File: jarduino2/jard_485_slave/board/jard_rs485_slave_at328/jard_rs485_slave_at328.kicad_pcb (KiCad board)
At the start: 2 copper layers, 80 x 30 mm, 72 parts, among them J1 BUS_IN, J2 BUS_OUT, J3 Débit, J4 Niveaux, J6 EV1, J7 ISCP, Q1 BPC_FMMT38C, Q2 BPC_FMMT38C, Q4 BPC_FMMT38C, Q6 BPC_IPP034N03L, U1 BPC_Alim5V, U2 MAX485E, U5 ATmega328P-A, U6 BPC_DHT22, Y1 Resonator

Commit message: Nouvel essai de routage avec en + LEDs
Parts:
- removed TP20, TP21: TestPoint, TestPoint:TestPoint_Pad_D1.5mm
- added D1: LED, LED_SMD:LED_0805_2012Metric_Pad1.15x1.40mm_HandSolder, B.Cu at (102.6, 44.6)
- added D3: LED, LED_THT:LED_D3.0mm_FlatTop, B.Cu at (103.8, 48.6)
- added R12: 220, Resistor_SMD:R_0805_2012Metric_Pad1.20x1.40mm_HandSolder, B.Cu at (87.8, 60.4)
- C13, C5, C8, C9, U5, Y1: moved to B.Cu
- R26: moved to F.Cu
- moved R17 40.5 mm to (125.2, 41.8), turned to 0 degrees
- moved TP11 38.2 mm to (80.4, 44.8), turned to 0 degrees
- moved Q6 38.0 mm to (126.3, 44.2), turned to 180 degrees
- moved D8 32.8 mm to (80.0, 48.9), turned to 90 degrees
- moved Y1 32.0 mm to (93.2, 67.2), turned to 0 degrees
- moved C8 31.2 mm to (93.6, 53.8), turned to 0 degrees
- moved Q4 29.4 mm to (116.1, 45.2), turned to 0 degrees
- moved R15 29.1 mm to (113.0, 45.2)
- moved D7 27.9 mm to (126.8, 67.5), turned to 180 degrees
- moved C9 26.5 mm to (95.9, 66.9)
- moved U5 25.7 mm to (96.3, 60.0)
- moved J6 25.6 mm to (121.2, 52.2), turned to 90 degrees
- moved C13 24.9 mm to (96.7, 53.9), turned to 180 degrees
- moved R7 24.8 mm to (84.4, 49.6), turned to 180 degrees
- moved R26 24.0 mm to (97.2, 60.4), turned to 180 degrees
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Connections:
- U5 pad 12: unconnected-(U5-PB0-Pad12) -> Net-(U5-PB0)
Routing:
- net +5V: track 234.6 -> 65.4 mm, vias 8 -> 0
- net TX_EN: track 87.6 -> 0.00 mm, vias 3 -> 0
- net RX: track 77.3 -> 1.78 mm, vias 3 -> 0
- net TX: track 73.7 -> 0.00 mm, vias 3 -> 0
- net CMD_EV1: track 56.8 -> 0.00 mm, vias 3 -> 0
- net TEMP: track 52.2 -> 0.00 mm, vias 6 -> 0
- net POW_MES: track 51.3 -> 0.00 mm, vias 2 -> 0
- net A3: track 39.1 -> 0.00 mm, vias 1 -> 0
- net RESET: track 34.7 -> 0.00 mm, vias 3 -> 0
- net GND: track 49.0 -> 15.3 mm, vias 29 -> 8
- net A1: track 27.5 -> 0.00 mm, vias 1 -> 0
- net LVL_HIGH: track 26.6 -> 0.00 mm, vias 1 -> 0
- net LVL_LOW: track 23.1 -> 0.00 mm, vias 1 -> 0
- net FLOW: track 21.6 -> 0.00 mm, vias 3 -> 0
- net MOSI: track 20.3 -> 0.00 mm
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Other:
- board text added: "VP"
- board text removed: "POWER_12V"
- board text removed: "Reset"
- board text removed: "TEMP"
- board text removed: "Vcc Prot."

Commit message: Routage...
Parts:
- moved R12 15.8 mm to (101.2, 52.2), turned to 90 degrees
- moved TP1 1.08 mm to (80.0, 52.5)
- moved TP4 1.00 mm to (80.0, 55.2)
- moved TP7 0.91 mm to (80.0, 58.0)
- moved R8 0.68 mm to (118.4, 62.0)
- moved D3 0.64 mm to (104.0, 48.0)
- moved R17 0.47 mm to (124.8, 41.7)
- moved R9 0.22 mm to (122.2, 66.7)
- moved D13 0.07 mm to (115.9, 49.7)
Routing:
- net +5V: track 65.4 -> 170.7 mm, vias 0 -> 9
- net TX: track 0.00 -> 53.0 mm, vias 0 -> 2
- net RX: track 1.78 -> 51.4 mm, vias 0 -> 2
- net TX_EN: track 0.00 -> 22.5 mm, vias 0 -> 2
- net LVL_HIGH: track 0.00 -> 22.2 mm, vias 0 -> 1
- net FLOW: track 0.00 -> 20.3 mm, vias 0 -> 3
- net Net-(Q4-C): track 0.00 -> 14.9 mm
- net POWER_12V: track 54.4 -> 68.7 mm, vias 0 -> 1
- net Net-(U5-PB0): track 0.00 -> 13.3 mm, vias 0 -> 1
- net Net-(J4-Pin_1): track 0.00 -> 12.6 mm
- net Net-(Q1-B): track 0.00 -> 11.5 mm, vias 0 -> 2
- net Net-(D13-K): track 0.00 -> 10.8 mm
- net VCC_PROTECTED: track 0.00 -> 9.62 mm
- net GND: track 15.3 -> 23.0 mm, vias 8 -> 14
- net Net-(D1-A): track 0.00 -> 6.74 mm
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
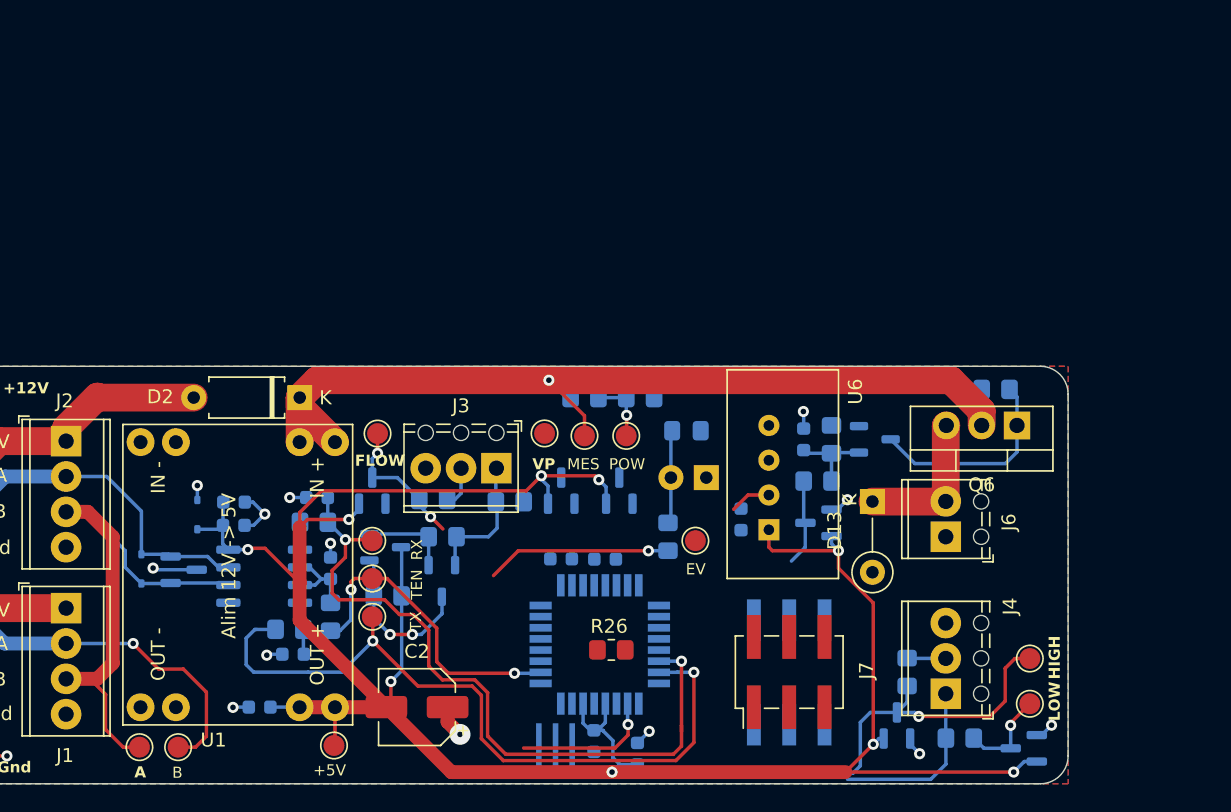
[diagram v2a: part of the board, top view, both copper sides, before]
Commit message: Re-routage en gagnant de la place (à finir)
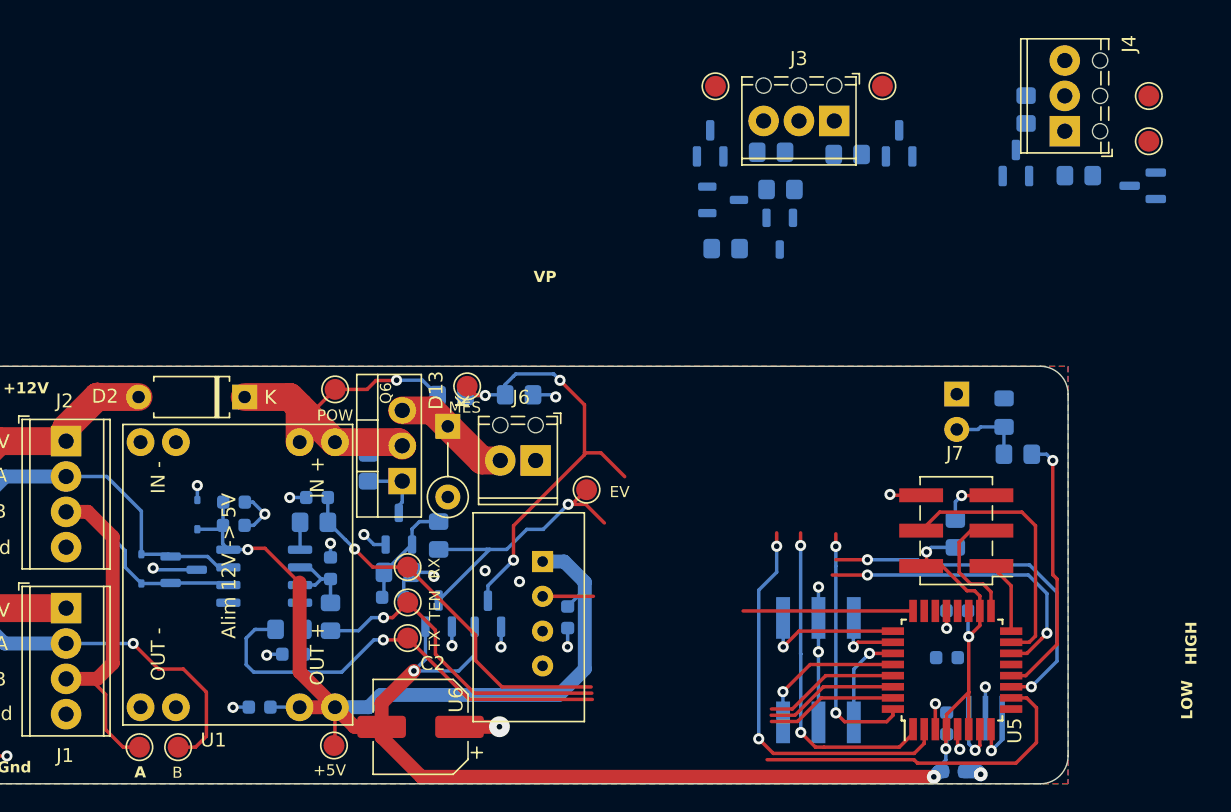
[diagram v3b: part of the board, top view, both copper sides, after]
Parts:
- C2: footprint Capacitor_SMD:CP_Elec_5x5.8 -> Capacitor_SMD:CP_Elec_6.3x5.2
- C5: value 1nF -> 100nF
- D2: value D -> SR560
- R26: moved to B.Cu
- U5: moved to F.Cu
- moved R17 45.4 mm to (79.7, 47.3), turned to -90 degrees
- moved Q6 44.4 mm to (82.2, 48.2), turned to 90 degrees
- moved D6 41.3 mm to (126.2, 25.4)
- moved D7 41.3 mm to (135.4, 27.0)
- moved J4 41.3 mm to (129.8, 23.1)
- moved R8 41.3 mm to (127.0, 21.6)
- moved R9 41.3 mm to (130.8, 26.3)
- moved TP12 41.3 mm to (135.8, 20.6)
- moved TP13 41.3 mm to (135.8, 23.8)
- moved D8 34.8 mm to (104.3, 24.0)
- moved D9 34.8 mm to (117.9, 24.0)
- moved J3 34.8 mm to (113.2, 22.4)
- moved Q1 34.8 mm to (105.2, 28.0)
- moved Q2 34.8 mm to (109.3, 30.5)
- moved R10 34.8 mm to (114.2, 24.8)
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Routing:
- net CMD_EV1: track 6.22 -> 46.8 mm, vias 0 -> 3
- net POW_MES: track 4.77 -> 44.9 mm, vias 1 -> 3
- net POWER_12V: track 68.7 -> 30.6 mm
- net GND: track 23.0 -> 49.8 mm, vias 14 -> 25
- net TX_EN: track 22.5 -> 48.0 mm, vias 2 -> 1
- net TEMP: track 2.96 -> 25.7 mm, vias 0 -> 2
- net MOSI: track 0.00 -> 19.0 mm
- net RX: track 51.4 -> 36.3 mm, vias 2 -> 1
- net RESET: track 0.00 -> 13.8 mm, vias 0 -> 1
- net Net-(J4-Pin_1): track 12.6 -> 0.00 mm
- net Net-(Q1-B): track 11.5 -> 0.00 mm, vias 2 -> 0
- net TX: track 53.0 -> 41.6 mm, vias 2 -> 1
- net LVL_LOW: track 6.73 -> 17.9 mm, vias 1 -> 2
- net A3: track 0.00 -> 10.9 mm, vias 0 -> 1
- net A2: track 0.00 -> 10.5 mm, vias 0 -> 1
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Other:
- board text removed: "FLOW"

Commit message: Fin du routage. Prêt pour revue.
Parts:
- D9, Q1, Q2, R10, R11, R6: moved to F.Cu
- moved TP14 40.7 mm to (106.0, 59.2)
- moved D9 40.1 mm to (98.1, 58.9), turned to 0 degrees
- moved TP12 39.3 mm to (111.8, 51.7)
- moved R10 36.7 mm to (102.5, 59.6), turned to 0 degrees
- moved R11 35.3 mm to (105.5, 62.4), turned to -90 degrees
- moved TP13 35.0 mm to (114.6, 51.7)
- moved Q1 35.0 mm to (98.2, 62.4), turned to 180 degrees
- moved R6 34.4 mm to (98.2, 65.2), turned to 0 degrees
- moved Q2 32.6 mm to (102.4, 62.4), turned to 0 degrees
- moved D6 32.3 mm to (108.5, 52.4)
- moved R8 32.2 mm to (112.5, 50.3)
- moved TP11 32.1 mm to (101.2, 51.8)
- moved R9 29.0 mm to (114.5, 50.3), turned to -90 degrees
- moved J4 28.5 mm to (113.9, 46.8), turned to 180 degrees
- moved D8 28.4 mm to (104.2, 52.4)
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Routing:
- net +5V: track 161.0 -> 230.5 mm, vias 6 -> 10
- net VCC_PROTECTED: track 0.00 -> 29.6 mm, vias 0 -> 2
- net POW_MES: track 44.9 -> 74.0 mm, vias 3 -> 4
- net CMD_EV1: track 46.8 -> 67.5 mm
- net TEMP: track 25.7 -> 44.8 mm
- net RX: track 36.3 -> 53.1 mm
- net TX: track 41.6 -> 58.0 mm, vias 1 -> 3
- net TX_EN: track 48.0 -> 63.3 mm
- net LVL_LOW: track 17.9 -> 28.0 mm
- net RESET: track 13.8 -> 21.4 mm, vias 1 -> 4
- net FLOW: track 29.0 -> 36.3 mm
- net LVL_HIGH: track 23.6 -> 30.7 mm
- net GND: track 49.8 -> 56.6 mm, vias 25 -> 29
- net Net-(Q1-B): track 0.00 -> 6.49 mm
- net Net-(Q1-E): track 0.00 -> 6.16 mm
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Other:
- board text added: "Esclave OYA Rev D0 BPC 2024"
- board text added: "FLOW"
- board text added: "PROT"
- board text removed: "Esclave OYA Rev C BPC 2024"
- board text removed: "VP"

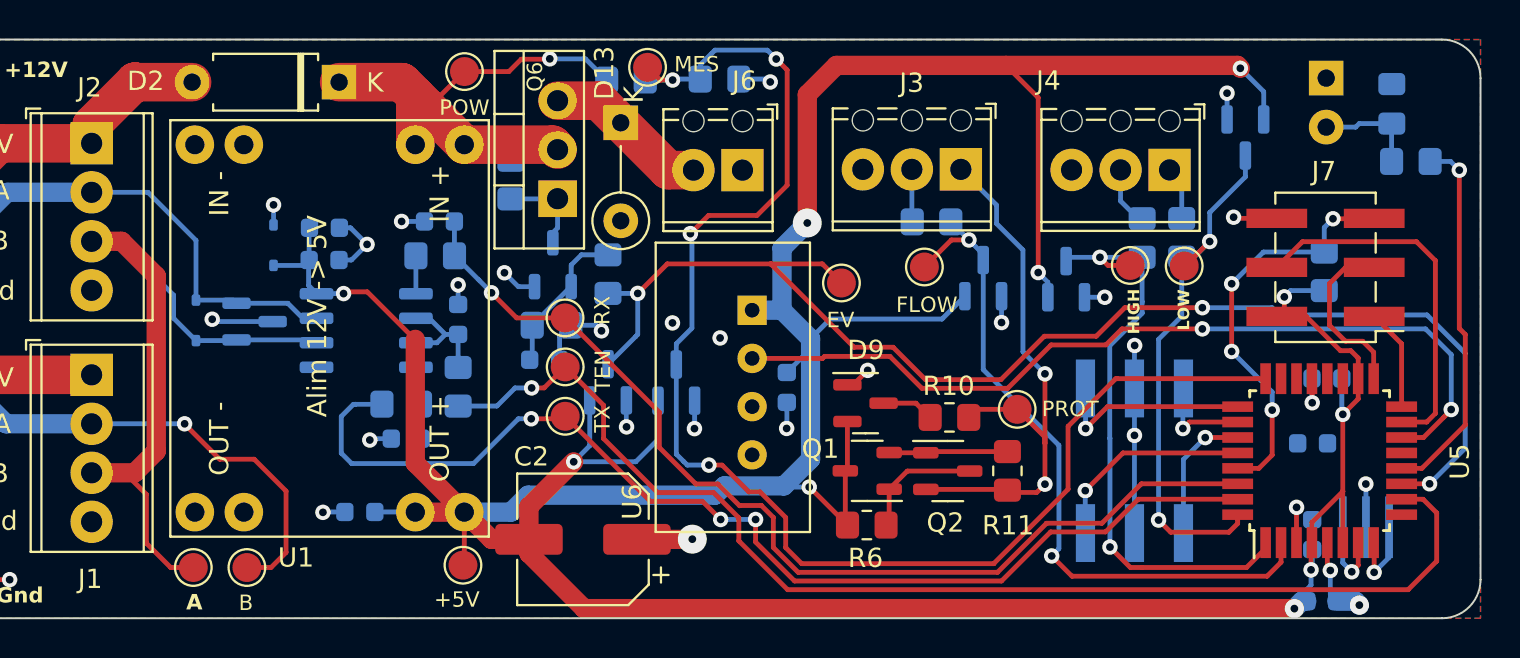
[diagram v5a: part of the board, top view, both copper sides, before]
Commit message: Suite revue: - Retrait limiteur de courant NOK pour flowmeter - Résolution des erreurs PCB
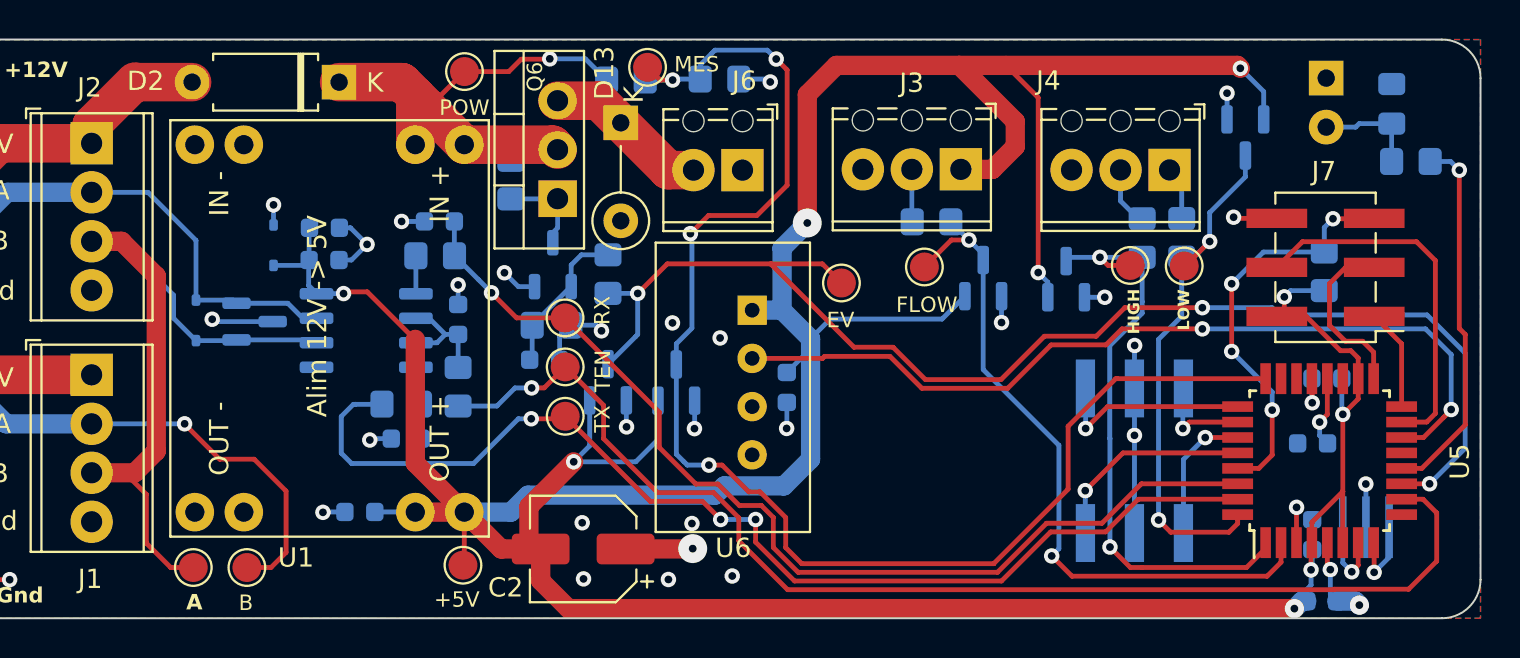
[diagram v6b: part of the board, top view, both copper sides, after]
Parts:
- removed D9: BAV99, Package_TO_SOT_SMD:SOT-23
- removed Q1, Q2: BPC_FMMT38C, bpc:BPC_SOT-23-3
- removed R10: 100, Resistor_SMD:R_0805_2012Metric_Pad1.20x1.40mm_HandSolder
- removed R11: 0.1, Resistor_SMD:R_0805_2012Metric_Pad1.20x1.40mm_HandSolder
- removed R6: 100k, Resistor_SMD:R_0805_2012Metric_Pad1.20x1.40mm_HandSolder
- removed TP14: TestPoint, TestPoint:TestPoint_Pad_D1.5mm
- C2: footprint Capacitor_SMD:CP_Elec_6.3x5.2 -> Capacitor_SMD:CP_Elec_5x5.9
- moved C2 0.50 mm to (83.5, 66.4)
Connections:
- J3 pad 1: VCC_PROTECTED -> +5V
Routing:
- net VCC_PROTECTED: track 29.6 -> 0.00 mm, vias 2 -> 0
- net +5V: track 230.5 -> 218.9 mm, vias 10 -> 9
- net Net-(Q1-B): track 6.49 -> 0.00 mm
- net Net-(Q1-E): track 6.16 -> 0.00 mm
- net Net-(U5-AREF): track 0.00 -> 3.69 mm, vias 0 -> 1
- net Net-(D9-K-Pad3): track 2.72 -> 0.00 mm
- net GND: track 56.6 -> 55.7 mm, vias 29 -> 33
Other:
- board text removed: "PROT"
